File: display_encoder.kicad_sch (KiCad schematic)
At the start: 9 parts, among them SW21 PEC11R, U21 Adafruit_PiOLED

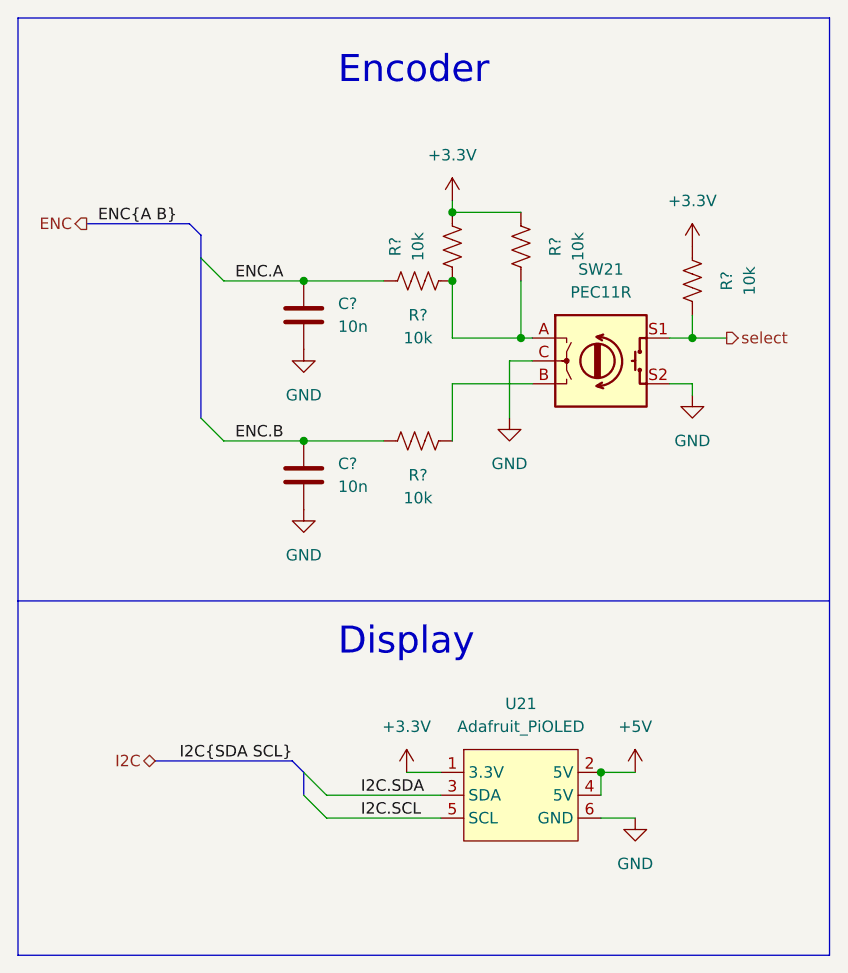
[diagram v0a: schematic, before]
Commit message: Add voltage reference and voltage regulator
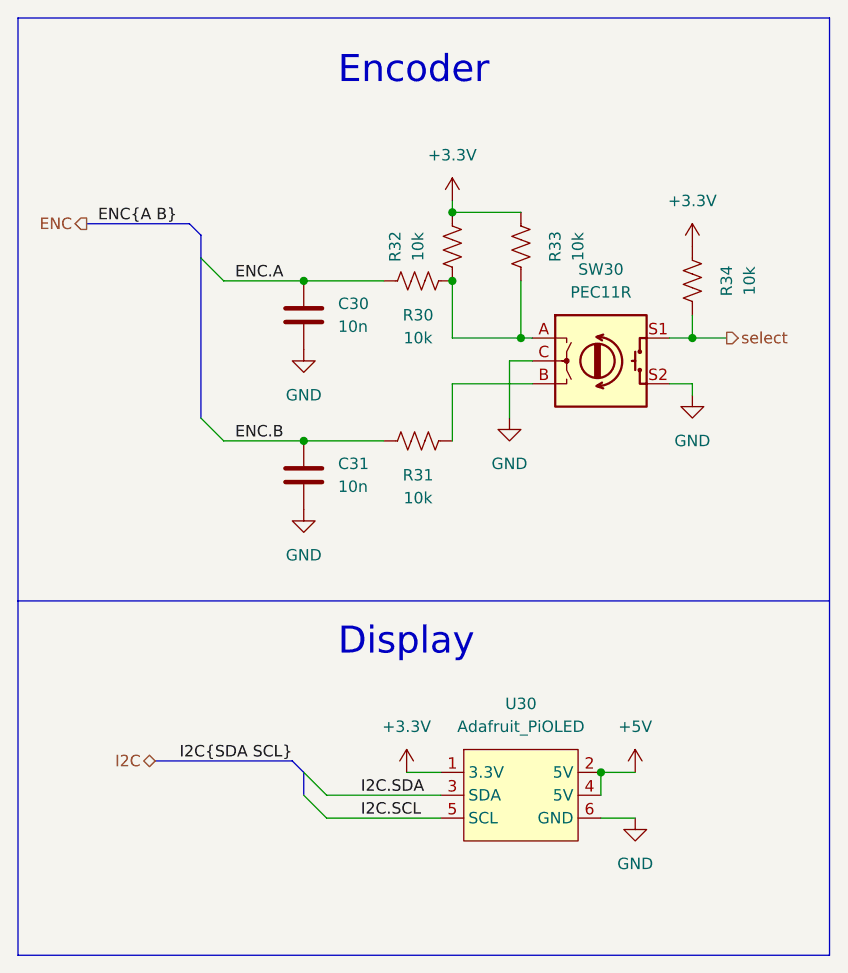
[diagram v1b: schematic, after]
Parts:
- gave numbers to parts that had none: 7
- renumbered SW21 to SW30, U21 to U30
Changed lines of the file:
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@@
   (symbol (lib_id "power:GND") (at 137.16 77.47 0) (unit 1)
     (in_bom yes) (on_board yes) (fields_autoplaced)
-    (property "Reference" "#PWR?" (id 0) (at 137.16 83.82 0)
+    (property "Reference" "#PWR0118" (id 0) (at 137.16 83.82 0)
       (effects (font (size 1.27 1.27)) hide)
     )
@@
   (symbol (lib_id "power:+3.3V") (at 180.34 66.04 0) (unit 1)
     (in_bom yes) (on_board yes) (fields_autoplaced)
-    (property "Reference" "#PWR?" (id 0) (at 180.34 69.85 0)
+    (property "Reference" "#PWR0120" (id 0) (at 180.34 69.85 0)
       (effects (font (size 1.27 1.27)) hide)
     )
@@
   (symbol (lib_id "Device:R_US") (at 149.86 69.85 90) (unit 1)
     (in_bom yes) (on_board yes)
-    (property "Reference" "R?" (id 0) (at 149.86 73.66 90))
+    (property "Reference" "R30" (id 0) (at 149.86 73.66 90))
     (property "Value" "10k" (id 1) (at 149.86 76.2 90))
     (property "Footprint" "Resistor_SMD:R_0805_2012Metric" (id 2) (at 150.114 68.834 90)
@@
   (symbol (lib_id "0_Display_Graphic:Adafruit_PiOLED") (at 161.29 127 0) (unit 1)
     (in_bom yes) (on_board yes) (fields_autoplaced)
-    (property "Reference" "U21" (id 0) (at 161.29 116.84 0))
+    (property "Reference" "U30" (id 0) (at 161.29 116.84 0))
     (property "Value" "Adafruit_PiOLED" (id 1) (at 161.29 119.38 0))
     (property "Footprint" "0_Display:PiOLED" (id 2) (at 162.56 121.92 0)
@@
   (symbol (lib_id "power:GND") (at 180.34 82.55 0) (unit 1)
     (in_bom yes) (on_board yes) (fields_autoplaced)
-    (property "Reference" "#PWR?" (id 0) (at 180.34 88.9 0)
+    (property "Reference" "#PWR0119" (id 0) (at 180.34 88.9 0)
       (effects (font (size 1.27 1.27)) hide)
     )
@@
   (symbol (lib_id "power:GND") (at 160.02 85.09 0) (unit 1)
     (in_bom yes) (on_board yes) (fields_autoplaced)
-    (property "Reference" "#PWR?" (id 0) (at 160.02 91.44 0)
+    (property "Reference" "#PWR0116" (id 0) (at 160.02 91.44 0)
       (effects (font (size 1.27 1.27)) hide)
     )
@@
   (symbol (lib_id "power:GND") (at 137.16 95.25 0) (unit 1)
     (in_bom yes) (on_board yes) (fields_autoplaced)
-    (property "Reference" "#PWR?" (id 0) (at 137.16 101.6 0)
+    (property "Reference" "#PWR0117" (id 0) (at 137.16 101.6 0)
       (effects (font (size 1.27 1.27)) hide)
     )
@@
   (symbol (lib_id "Device:C") (at 137.16 73.66 180) (unit 1)
     (in_bom yes) (on_board yes) (fields_autoplaced)
-    (property "Reference" "C?" (id 0) (at 140.97 72.3899 0)
+    (property "Reference" "C30" (id 0) (at 140.97 72.3899 0)
       (effects (font (size 1.27 1.27)) (justify right))
     )
@@
   (symbol (lib_id "Device:RotaryEncoder_Switch") (at 170.18 78.74 0) (unit 1)
     (in_bom yes) (on_board yes)
-    (property "Reference" "SW21" (id 0) (at 170.18 68.58 0))
+    (property "Reference" "SW30" (id 0) (at 170.18 68.58 0))
     (property "Value" "PEC11R" (id 1) (at 170.18 71.12 0))
     (property "Footprint" "" (id 2) (at 166.37 74.676 0)
@@
   (symbol (lib_id "Device:C") (at 137.16 91.44 180) (unit 1)
     (in_bom yes) (on_board yes) (fields_autoplaced)
-    (property "Reference" "C?" (id 0) (at 140.97 90.1699 0)
+    (property "Reference" "C31" (id 0) (at 140.97 90.1699 0)
       (effects (font (size 1.27 1.27)) (justify right))
     )
@@
   (symbol (lib_id "Device:R_US") (at 153.67 66.04 0) (unit 1)
     (in_bom yes) (on_board yes)
-    (property "Reference" "R?" (id 0) (at 147.32 66.04 90))
+    (property "Reference" "R32" (id 0) (at 147.32 66.04 90))
     (property "Value" "10k" (id 1) (at 149.86 66.04 90))
     (property "Footprint" "Resistor_SMD:R_0805_2012Metric" (id 2) (at 154.686 66.294 90)
@@
   (symbol (lib_id "Device:R_US") (at 180.34 69.85 180) (unit 1)
     (in_bom yes) (on_board yes)
-    (property "Reference" "R?" (id 0) (at 184.15 69.85 90))
+    (property "Reference" "R34" (id 0) (at 184.15 69.85 90))
     (property "Value" "10k" (id 1) (at 186.69 69.85 90))
     (property "Footprint" "Resistor_SMD:R_0805_2012Metric" (id 2) (at 179.324 69.596 90)
@@
   (symbol (lib_id "Device:R_US") (at 149.86 87.63 90) (unit 1)
     (in_bom yes) (on_board yes)
-    (property "Reference" "R?" (id 0) (at 149.86 91.44 90))
+    (property "Reference" "R31" (id 0) (at 149.86 91.44 90))
     (property "Value" "10k" (id 1) (at 149.86 93.98 90))
     (property "Footprint" "Resistor_SMD:R_0805_2012Metric" (id 2) (at 150.114 86.614 90)
@@
   (symbol (lib_id "power:+3.3V") (at 153.67 60.96 0) (unit 1)
     (in_bom yes) (on_board yes) (fields_autoplaced)
-    (property "Reference" "#PWR?" (id 0) (at 153.67 64.77 0)
+    (property "Reference" "#PWR0115" (id 0) (at 153.67 64.77 0)
       (effects (font (size 1.27 1.27)) hide)
     )
@@
   (symbol (lib_id "Device:R_US") (at 161.29 66.04 180) (unit 1)
     (in_bom yes) (on_board yes)
-    (property "Reference" "R?" (id 0) (at 165.1 66.04 90))
+    (property "Reference" "R33" (id 0) (at 165.1 66.04 90))
     (property "Value" "10k" (id 1) (at 167.64 66.04 90))
     (property "Footprint" "Resistor_SMD:R_0805_2012Metric" (id 2) (at 160.274 65.786 90)

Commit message: Fix lots of small things
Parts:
- SW30: footprint (none) -> Rotary_Encoder:RotaryEncoder_Alps_EC12E-Switch_Vertical_H20mm
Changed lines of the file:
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@@
     (property "Reference" "SW30" (id 0) (at 170.18 68.58 0))
     (property "Value" "PEC11R" (id 1) (at 170.18 71.12 0))
-    (property "Footprint" "" (id 2) (at 166.37 74.676 0)
+    (property "Footprint" "Rotary_Encoder:RotaryEncoder_Alps_EC12E-Switch_Vertical_H20mm" (id 2) (at 166.37 74.676 0)
       (effects (font (size 1.27 1.27)) hide)
     )

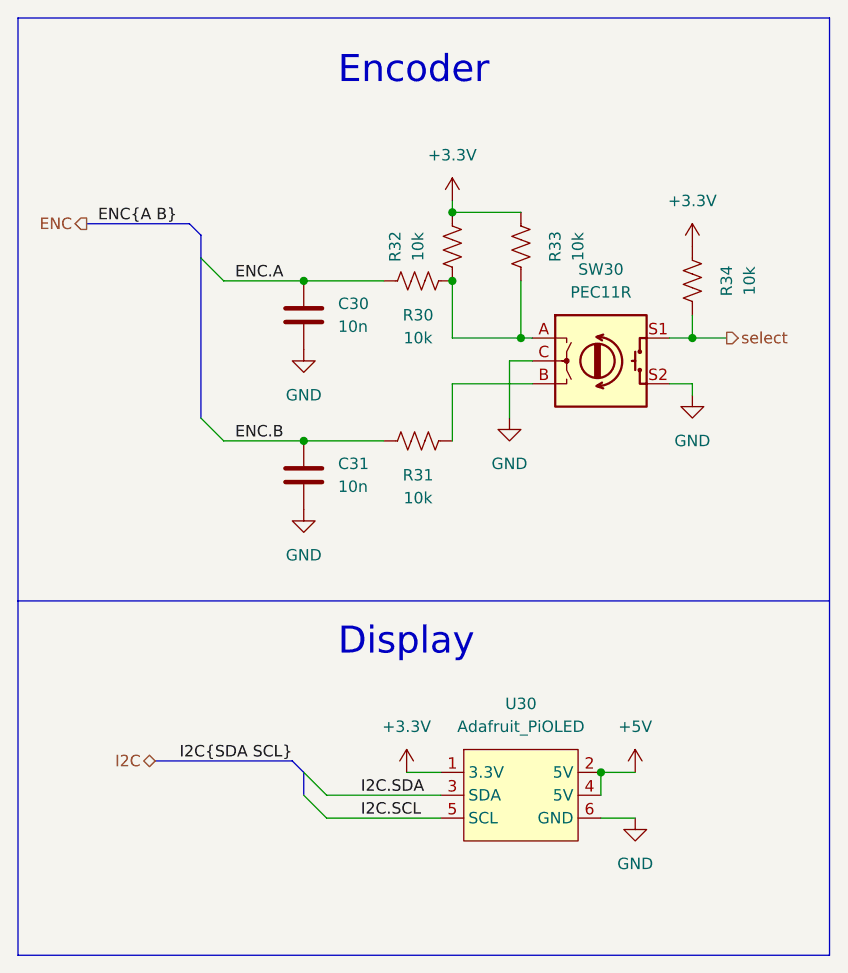
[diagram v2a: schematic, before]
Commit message: Arrange components of subcircuits
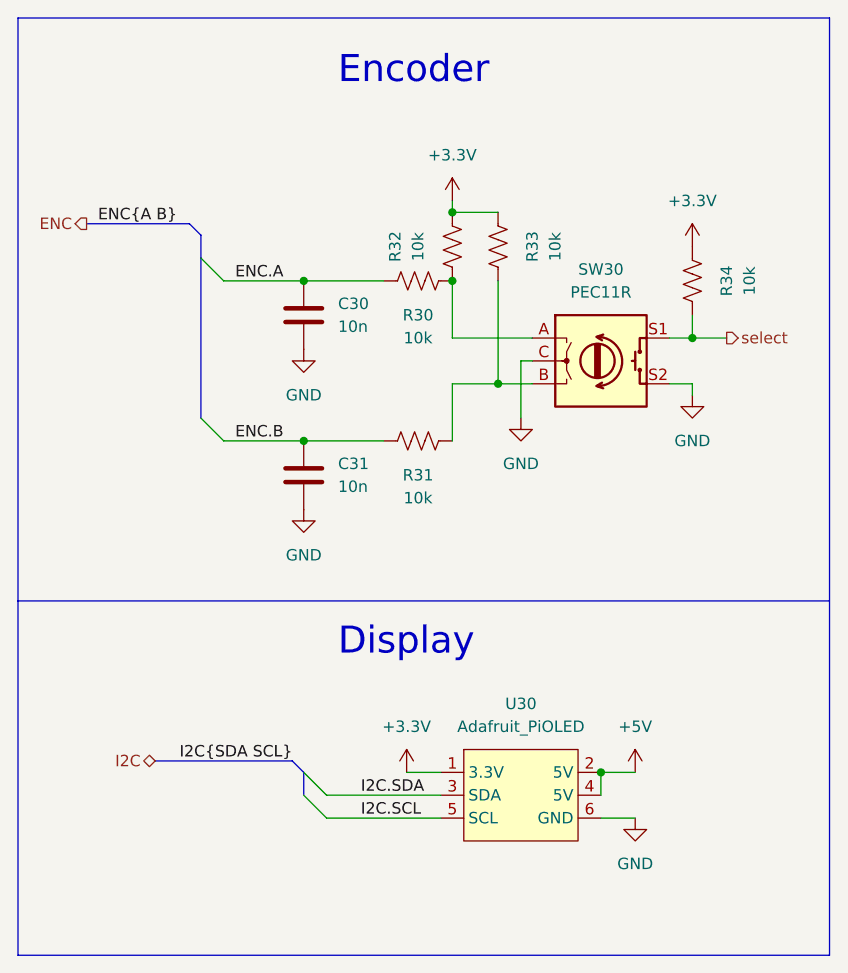
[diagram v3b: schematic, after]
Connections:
- net at R30.2, R32.2, SW30.A: no longer R33.1
- net at R31.2, SW30.B: now also R33.1
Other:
- moved on the sheet: R33
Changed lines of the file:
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@@
 (kicad_sch (version 20211123) (generator eeschema)
   (paper "A4")
-  (junction (at 161.29 76.2) (diameter 0) (color 0 0 0 0)
-  )
   (junction (at 137.16 87.63) (diameter 0) (color 0 0 0 0)
   )
@@
   (junction (at 137.16 69.85) (diameter 0) (color 0 0 0 0)
   )
+  (junction (at 158.75 81.28) (diameter 0) (color 0 0 0 0)
+  )
   (junction (at 170.18 124.46) (diameter 0) (color 0 0 0 0)
   )
@@
     (stroke (width 0) (type default) (color 0 0 0 0))
   )
-  (wire (pts (xy 162.56 76.2) (xy 161.29 76.2))
+  (wire (pts (xy 153.67 76.2) (xy 162.56 76.2))
     (stroke (width 0) (type default) (color 0 0 0 0))
   )
@@
     (stroke (width 0) (type default) (color 0 0 0 0))
   )
+  (wire (pts (xy 158.75 69.85) (xy 158.75 81.28))
+    (stroke (width 0) (type default) (color 0 0 0 0))
+  )
   (wire (pts (xy 177.8 76.2) (xy 180.34 76.2))
     (stroke (width 0) (type default) (color 0 0 0 0))
   )
+  (wire (pts (xy 158.75 81.28) (xy 153.67 81.28))
+    (stroke (width 0) (type default) (color 0 0 0 0))
+  )
   (wire (pts (xy 170.18 129.54) (xy 173.99 129.54))
     (stroke (width 0) (type default) (color 0 0 0 0))
@@
     (stroke (width 0) (type default) (color 0 0 0 0))
   )
-  (wire (pts (xy 162.56 81.28) (xy 153.67 81.28))
+  (wire (pts (xy 162.56 81.28) (xy 158.75 81.28))
     (stroke (width 0) (type default) (color 0 0 0 0))
   )
@@
     (stroke (width 0) (type default) (color 0 0 0 0))
   )
-  (wire (pts (xy 160.02 85.09) (xy 160.02 78.74))
-    (stroke (width 0) (type default) (color 0 0 0 0))
-  )
-  (wire (pts (xy 161.29 76.2) (xy 153.67 76.2))
+  (wire (pts (xy 161.29 85.09) (xy 161.29 78.74))
     (stroke (width 0) (type default) (color 0 0 0 0))
   )
@@
     (stroke (width 0) (type default) (color 0 0 0 0))
   )
-  (wire (pts (xy 161.29 69.85) (xy 161.29 76.2))
-    (stroke (width 0) (type default) (color 0 0 0 0))
-  )
   (wire (pts (xy 153.67 76.2) (xy 153.67 69.85))
     (stroke (width 0) (type default) (color 0 0 0 0))
   )
-  (wire (pts (xy 160.02 78.74) (xy 162.56 78.74))
+  (wire (pts (xy 161.29 78.74) (xy 162.56 78.74))
     (stroke (width 0) (type default) (color 0 0 0 0))
   )
@@
     (stroke (width 0) (type default) (color 0 0 0 0))
   )
-  (wire (pts (xy 153.67 62.23) (xy 161.29 62.23))
+  (wire (pts (xy 153.67 62.23) (xy 158.75 62.23))
     (stroke (width 0) (type default) (color 0 0 0 0))
   )
@@
     (pin "1")
   )
-  (symbol (lib_id "power:GND") (at 160.02 85.09 0) (unit 1)
-    (in_bom yes) (on_board yes) (fields_autoplaced)
-    (property "Reference" "#PWR0116" (id 0) (at 160.02 91.44 0)
-      (effects (font (size 1.27 1.27)) hide)
-    )
-    (property "Value" "GND" (id 1) (at 160.02 90.17 0))
-    (property "Footprint" "" (id 2) (at 160.02 85.09 0)
-      (effects (font (size 1.27 1.27)) hide)
-    )
-    (property "Datasheet" "" (id 3) (at 160.02 85.09 0)
+  (symbol (lib_id "power:GND") (at 161.29 85.09 0) (unit 1)
+    (in_bom yes) (on_board yes) (fields_autoplaced)
+    (property "Reference" "#PWR0116" (id 0) (at 161.29 91.44 0)
+      (effects (font (size 1.27 1.27)) hide)
+    )
+    (property "Value" "GND" (id 1) (at 161.29 90.17 0))
+    (property "Footprint" "" (id 2) (at 161.29 85.09 0)
+      (effects (font (size 1.27 1.27)) hide)
+    )
+    (property "Datasheet" "" (id 3) (at 161.29 85.09 0)
       (effects (font (size 1.27 1.27)) hide)
     )
@@
     (pin "1")
   )
-  (symbol (lib_id "Device:R_US") (at 161.29 66.04 180) (unit 1)
-    (in_bom yes) (on_board yes)
-    (property "Reference" "R33" (id 0) (at 165.1 66.04 90))
-    (property "Value" "10k" (id 1) (at 167.64 66.04 90))
-    (property "Footprint" "Resistor_SMD:R_0805_2012Metric" (id 2) (at 160.274 65.786 90)
-      (effects (font (size 1.27 1.27)) hide)
-    )
-    (property "Datasheet" "~" (id 3) (at 161.29 66.04 0)
-      (effects (font (size 1.27 1.27)) hide)
-    )
+  (symbol (lib_id "Device:R_US") (at 158.75 66.04 180) (unit 1)
+    (in_bom yes) (on_board yes)
+    (property "Reference" "R33" (id 0) (at 162.56 66.04 90))
+    (property "Value" "10k" (id 1) (at 165.1 66.04 90))
+    (property "Footprint" "Resistor_SMD:R_0805_2012Metric" (id 2) (at 157.734 65.786 90)
+      (effects (font (size 1.27 1.27)) hide)
+    )
+    (property "Datasheet" "~" (id 3) (at 158.75 66.04 0)
+      (effects (font (size 1.27 1.27)) hide)
+    )

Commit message: WIP PCB Routing
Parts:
- C30, C31: value 10n -> (none); footprint Capacitor_SMD:C_0805_2012Metric -> (none)
- R30, R31, R32, R33, R34: value 10k -> (none); footprint Resistor_SMD:R_0805_2012Metric -> (none)
- SW30: value PEC11R -> (none); footprint Rotary_Encoder:RotaryEncoder_Alps_EC12E-Switch_Vertical_H20mm -> (none)
- U30: value Adafruit_PiOLED -> (none); footprint 0_Display:PiOLED -> (none)
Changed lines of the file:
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@@
     (in_bom yes) (on_board yes)
     (property "Reference" "R30" (id 0) (at 149.86 73.66 90))
-    (property "Value" "10k" (id 1) (at 149.86 76.2 90))
-    (property "Footprint" "Resistor_SMD:R_0805_2012Metric" (id 2) (at 150.114 68.834 90)
+    (property "Value" "" (id 1) (at 149.86 76.2 90))
+    (property "Footprint" "" (id 2) (at 150.114 68.834 90)
       (effects (font (size 1.27 1.27)) hide)
     )
@@
     (in_bom yes) (on_board yes) (fields_autoplaced)
     (property "Reference" "U30" (id 0) (at 161.29 116.84 0))
-    (property "Value" "Adafruit_PiOLED" (id 1) (at 161.29 119.38 0))
-    (property "Footprint" "0_Display:PiOLED" (id 2) (at 162.56 121.92 0)
+    (property "Value" "" (id 1) (at 161.29 119.38 0))
+    (property "Footprint" "" (id 2) (at 162.56 121.92 0)
       (effects (font (size 1.27 1.27)) hide)
     )
@@
       (effects (font (size 1.27 1.27)) (justify right))
     )
-    (property "Value" "10n" (id 1) (at 140.97 74.9299 0)
-      (effects (font (size 1.27 1.27)) (justify right))
-    )
-    (property "Footprint" "Capacitor_SMD:C_0805_2012Metric" (id 2) (at 136.1948 69.85 0)
+    (property "Value" "" (id 1) (at 140.97 74.9299 0)
+      (effects (font (size 1.27 1.27)) (justify right))
+    )
+    (property "Footprint" "" (id 2) (at 136.1948 69.85 0)
       (effects (font (size 1.27 1.27)) hide)
     )
@@
     (in_bom yes) (on_board yes)
     (property "Reference" "SW30" (id 0) (at 170.18 68.58 0))
-    (property "Value" "PEC11R" (id 1) (at 170.18 71.12 0))
-    (property "Footprint" "Rotary_Encoder:RotaryEncoder_Alps_EC12E-Switch_Vertical_H20mm" (id 2) (at 166.37 74.676 0)
+    (property "Value" "" (id 1) (at 170.18 71.12 0))
+    (property "Footprint" "" (id 2) (at 166.37 74.676 0)
       (effects (font (size 1.27 1.27)) hide)
     )
@@
       (effects (font (size 1.27 1.27)) (justify right))
     )
-    (property "Value" "10n" (id 1) (at 140.97 92.7099 0)
-      (effects (font (size 1.27 1.27)) (justify right))
-    )
-    (property "Footprint" "Capacitor_SMD:C_0805_2012Metric" (id 2) (at 136.1948 87.63 0)
+    (property "Value" "" (id 1) (at 140.97 92.7099 0)
+      (effects (font (size 1.27 1.27)) (justify right))
+    )
+    (property "Footprint" "" (id 2) (at 136.1948 87.63 0)
       (effects (font (size 1.27 1.27)) hide)
     )
@@
     (in_bom yes) (on_board yes)
     (property "Reference" "R32" (id 0) (at 147.32 66.04 90))
-    (property "Value" "10k" (id 1) (at 149.86 66.04 90))
-    (property "Footprint" "Resistor_SMD:R_0805_2012Metric" (id 2) (at 154.686 66.294 90)
+    (property "Value" "" (id 1) (at 149.86 66.04 90))
+    (property "Footprint" "" (id 2) (at 154.686 66.294 90)
       (effects (font (size 1.27 1.27)) hide)
     )
@@
     (in_bom yes) (on_board yes)
     (property "Reference" "R34" (id 0) (at 184.15 69.85 90))
-    (property "Value" "10k" (id 1) (at 186.69 69.85 90))
-    (property "Footprint" "Resistor_SMD:R_0805_2012Metric" (id 2) (at 179.324 69.596 90)
+    (property "Value" "" (id 1) (at 186.69 69.85 90))
+    (property "Footprint" "" (id 2) (at 179.324 69.596 90)
       (effects (font (size 1.27 1.27)) hide)
     )
@@
     (in_bom yes) (on_board yes)
     (property "Reference" "R31" (id 0) (at 149.86 91.44 90))
-    (property "Value" "10k" (id 1) (at 149.86 93.98 90))
-    (property "Footprint" "Resistor_SMD:R_0805_2012Metric" (id 2) (at 150.114 86.614 90)
+    (property "Value" "" (id 1) (at 149.86 93.98 90))
+    (property "Footprint" "" (id 2) (at 150.114 86.614 90)
       (effects (font (size 1.27 1.27)) hide)
     )
@@
     (in_bom yes) (on_board yes)
     (property "Reference" "R33" (id 0) (at 162.56 66.04 90))
-    (property "Value" "10k" (id 1) (at 165.1 66.04 90))
-    (property "Footprint" "Resistor_SMD:R_0805_2012Metric" (id 2) (at 157.734 65.786 90)
-      (effects (font (size 1.27 1.27)) hide)
-    )
+    (property "Value" "" (id 1) (at 165.1 66.04 90))
+    (property "Footprint" "" (id 2) (at 157.734 65.786 90)
+      (effects (font (size 1.27 1.27)) hide)
+    )
